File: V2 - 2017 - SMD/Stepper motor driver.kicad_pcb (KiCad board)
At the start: 2 copper layers, 32.5 x 19.1 mm, 21 parts, among them P1 CONN_01X04, P2 CONN_01X03, P3 CONN_01X03, Q1 TIP120, Q2 TIP120, Q3 TIP120, Q4 TIP120, U1 74LS175, U2 74LS157

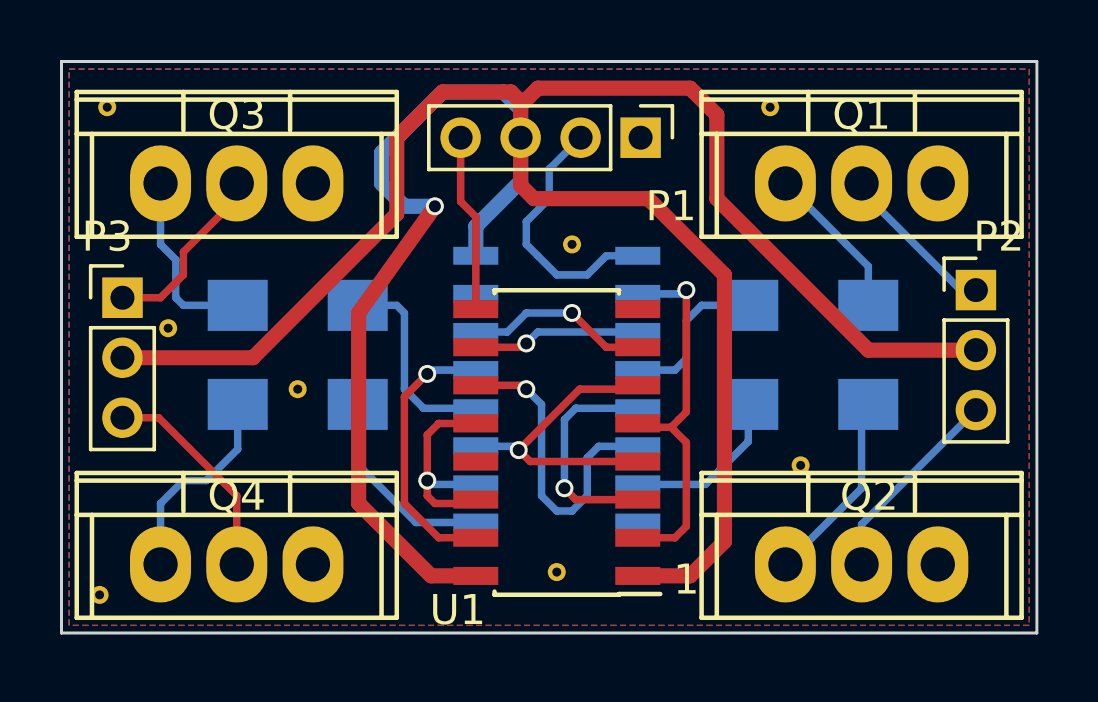
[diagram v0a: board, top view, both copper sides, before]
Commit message: Small changes
Added some measurements on the PCB, fixed up visual elements
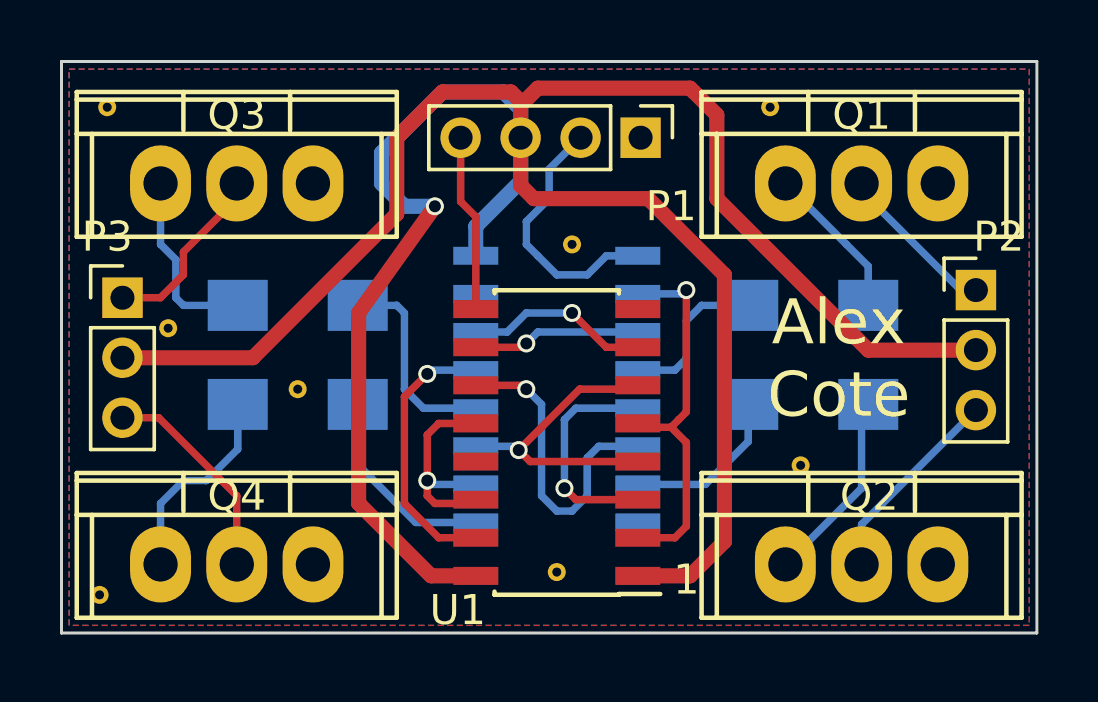
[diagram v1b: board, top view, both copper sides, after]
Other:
- board text added: "Alex Cote"
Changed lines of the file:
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@@
     (links 46)
     (no_connects 1)
-    (area 125.701667 73.885666 179.352334 105.115)
+    (area 125.701667 73.885666 179.352334 106.934001)
     (thickness 1.6)
-    (drawings 6)
+    (drawings 11)
     (tracks 159)
     (zones 0)
@@
   (layers
     (0 F.Cu signal)
-    (31 B.Cu signal)
-    (32 B.Adhes user)
+    (31 B.Cu signal hide)
+    (32 B.Adhes user hide)
     (33 F.Adhes user)
     (34 B.Paste user hide)
@@
     (39 F.Mask user)
     (40 Dwgs.User user)
-    (41 Cmts.User user hide)
+    (41 Cmts.User user)
     (42 Eco1.User user)
     (43 Eco2.User user)
@@
     (pad_to_mask_clearance 0)
     (aux_axis_origin 0 0)
-    (visible_elements 7FFFFB9F)
+    (visible_elements 7FFDFA9F)
     (pcbplotparams
       (layerselection 0x00030_80000001)
@@
     )
   )
+  (dimension 19.05 (width 0.3) (layer F.SilkS)
+    (gr_text "19.050 mm" (at 173.308 93.345 90) (layer F.SilkS)
+      (effects (font (size 1.5 1.5) (thickness 0.3)))
+    )
+    (feature1 (pts (xy 169.926 83.82) (xy 174.658 83.82)))
+    (feature2 (pts (xy 169.926 102.87) (xy 174.658 102.87)))
+    (crossbar (pts (xy 171.958 102.87) (xy 171.958 83.82)))
+    (arrow1a (pts (xy 171.958 83.82) (xy 172.544421 84.946504)))
+    (arrow1b (pts (xy 171.958 83.82) (xy 171.371579 84.946504)))
+    (arrow2a (pts (xy 171.958 102.87) (xy 172.544421 101.743496)))
+    (arrow2b (pts (xy 171.958 102.87) (xy 171.371579 101.743496)))
+  )
+  (dimension 32.512 (width 0.3) (layer F.SilkS)
+    (gr_text "32.512 mm" (at 152.654 106.252) (layer F.SilkS)
+      (effects (font (size 1.5 1.5) (thickness 0.3)))
+    )
+    (feature1 (pts (xy 168.91 104.14) (xy 168.91 107.602)))
+    (feature2 (pts (xy 136.398 104.14) (xy 136.398 107.602)))
+    (crossbar (pts (xy 136.398 104.902) (xy 168.91 104.902)))
+    (arrow1a (pts (xy 168.91 104.902) (xy 167.783496 105.488421)))
+    (arrow1b (pts (xy 168.91 104.902) (xy 167.783496 104.315579)))
+    (arrow2a (pts (xy 136.398 104.902) (xy 137.524504 105.488421)))
+    (arrow2b (pts (xy 136.398 104.902) (xy 137.524504 104.315579)))
+  )
+  (gr_text "Alex \nCote" (at 162.306 93.726) (layer F.SilkS)
+    (effects (font (size 1.5 1.5) (thickness 0.3)))
+  )
+  (dimension 19.05 (width 0.3) (layer B.SilkS)
+    (gr_text "19.050 mm" (at 172.546 93.345 90) (layer B.SilkS)
+      (effects (font (size 1.5 1.5) (thickness 0.3)))
+    )
+    (feature1 (pts (xy 169.672 83.82) (xy 173.896 83.82)))
+    (feature2 (pts (xy 169.672 102.87) (xy 173.896 102.87)))
+    (crossbar (pts (xy 171.196 102.87) (xy 171.196 83.82)))
+    (arrow1a (pts (xy 171.196 83.82) (xy 171.782421 84.946504)))
+    (arrow1b (pts (xy 171.196 83.82) (xy 170.609579 84.946504)))
+    (arrow2a (pts (xy 171.196 102.87) (xy 171.782421 101.743496)))
+    (arrow2b (pts (xy 171.196 102.87) (xy 170.609579 101.743496)))
+  )
+  (dimension 32.512 (width 0.3) (layer B.SilkS)
+    (gr_text "32.512 mm" (at 152.654 105.664) (layer B.SilkS)
+      (effects (font (size 1.5 1.5) (thickness 0.3)))
+    )
+    (feature1 (pts (xy 168.91 106.934) (xy 168.91 106.934)))
+    (feature2 (pts (xy 136.398 106.934) (xy 136.398 106.934)))
+    (crossbar (pts (xy 136.398 106.934) (xy 168.91 106.934)))
+    (arrow1a (pts (xy 168.91 106.934) (xy 167.783496 107.520421)))
+    (arrow1b (pts (xy 168.91 106.934) (xy 167.783496 106.347579)))
+    (arrow2a (pts (xy 136.398 106.934) (xy 137.524504 107.520421)))
+    (arrow2b (pts (xy 136.398 106.934) (xy 137.524504 106.347579)))
+  )
   (gr_text 1 (at 157.226 90.17) (layer B.SilkS)
